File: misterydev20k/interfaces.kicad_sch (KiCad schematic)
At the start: 57 parts, among them J11 Joystick 0, J12 Joystick 1, J4 Micro_SD_Card_Det1, J5 HDMI_A, J6 Grove 1125S-4P, SW2 KEY1, SW3 KEY2, U10 74LCX07, U9 74LCX07

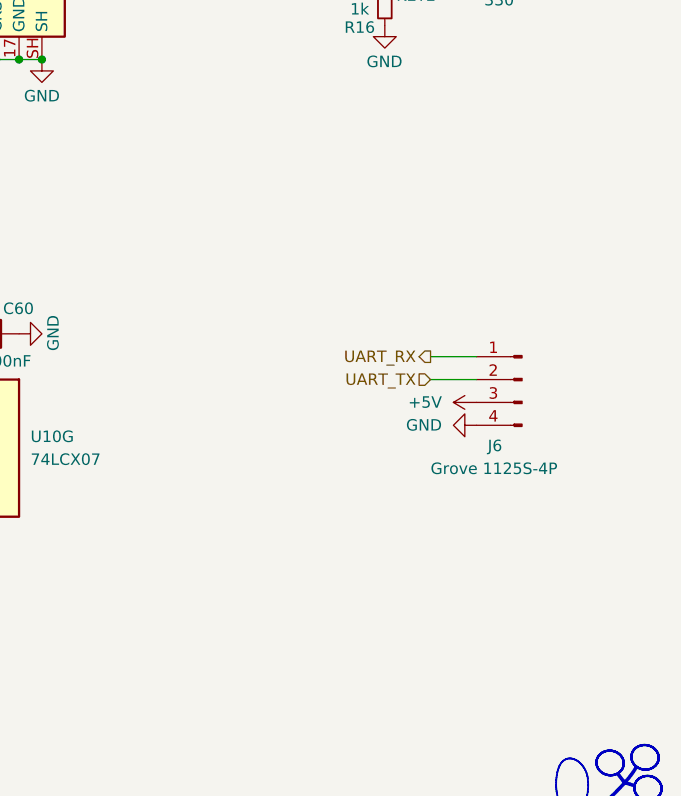
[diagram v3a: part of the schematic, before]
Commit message: Update debug UART wiring
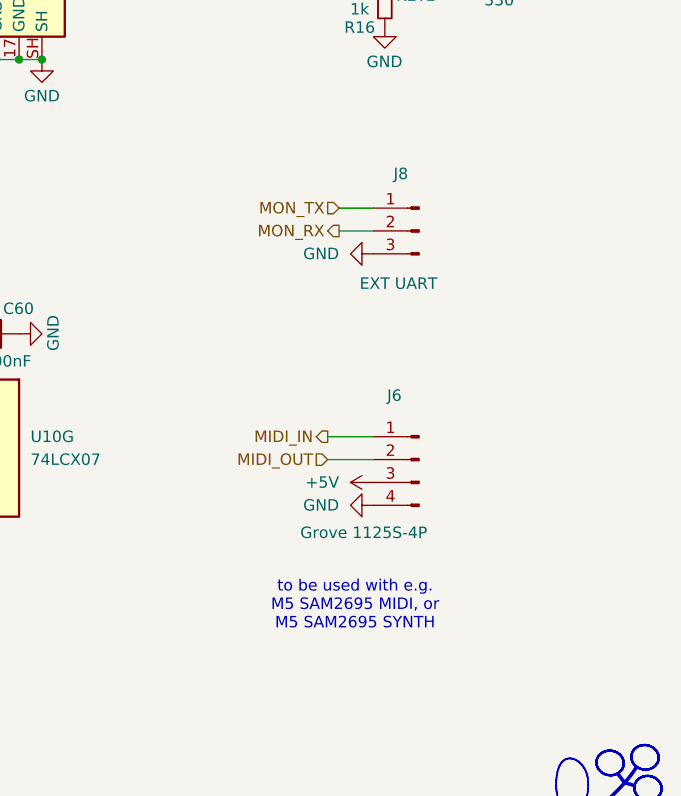
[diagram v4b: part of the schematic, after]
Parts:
- added J8: EXT UART, Connector_PinHeader_2.54mm:PinHeader_1x03_P2.54mm_Vertical, symbol Connector:Conn_01x03_Pin
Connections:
- net GND: now also J8.3 (Pin_3)
- net UART_RX renamed MIDI_IN
- net UART_TX renamed MIDI_OUT
- new net MON_RX: J8.2 (Pin_2)
- new net MON_TX: J8.1 (Pin_1)
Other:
- note added: "to be used with e.g. M5 SAM2695 MIDI, or M5 SAM2695 SYNTH"
- moved on the sheet: J6
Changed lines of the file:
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@@
 		)
 	)
+	(text "to be used with e.g.\nM5 SAM2695 MIDI, or\nM5 SAM2695 SYNTH"
+		(exclude_from_sim no)
+		(at 249.428 152.146 0)
+		(effects
+			(font
+				(size 1.27 1.27)
+			)
+		)
+	)
 	(text "DOWN"
 		(exclude_from_sim no)
@@
 	(wire
 		(pts
-			(xy 257.81 124.46) (xy 262.89 124.46)
+			(xy 246.38 133.35) (xy 251.46 133.35)
 		)
 		(stroke
@@
 	(wire
 		(pts
+			(xy 247.65 107.95) (xy 251.46 107.95)
+		)
+		(stroke
+			(width 0)
+			(type default)
+		)
+	)
+	(wire
+		(pts
 			(xy 54.61 31.75) (xy 55.88 31.75)
 		)
@@
 	(wire
 		(pts
+			(xy 247.65 110.49) (xy 251.46 110.49)
+		)
+		(stroke
+			(width 0)
+			(type default)
+		)
+	)
+	(wire
+		(pts
 			(xy 138.43 128.27) (xy 128.27 128.27)
 		)
@@
 	(wire
 		(pts
-			(xy 257.81 127) (xy 262.89 127)
+			(xy 246.38 135.89) (xy 251.46 135.89)
 		)
 		(stroke
@@
 		)
 	)
-	(hierarchical_label "UART_RX"
+	(hierarchical_label "MIDI_IN"
 		(shape output)
-		(at 257.81 124.46 180)
+		(at 246.38 133.35 180)
 		(effects
 			(font
@@
 		)
 	)
-	(hierarchical_label "UART_TX"
+	(hierarchical_label "MIDI_OUT"
 		(shape input)
-		(at 257.81 127 180)
+		(at 246.38 135.89 180)
 		(effects
 			(font
@@
 		)
 	)
+	(hierarchical_label "MON_RX"
+		(shape output)
+		(at 247.65 110.49 180)
+		(effects
+			(font
+				(size 1.27 1.27)
+			)
+			(justify right)
+		)
+	)
+	(hierarchical_label "MON_TX"
+		(shape input)
+		(at 247.65 107.95 180)
+		(effects
+			(font
+				(size 1.27 1.27)
+			)
+			(justify right)
+		)
+	)
 	(hierarchical_label "SD_DAT3"
 		(shape bidirectional)
@@
 	(symbol
 		(lib_id "power:GND")
-		(at 262.89 132.08 270)
+		(at 251.46 140.97 270)
 		(unit 1)
 		(exclude_from_sim no)
@@
 		(dnp no)
 		(property "Reference" "#PWR0110"
-			(at 256.54 132.08 0)
+			(at 245.11 140.97 0)
 			(effects
 				(font
@@
 		)
 		(property "Value" "GND"
-			(at 259.08 132.08 90)
+			(at 247.65 140.97 90)
 			(effects
 				(font
@@
 		)
 		(property "Footprint" ""
-			(at 262.89 132.08 0)
+			(at 251.46 140.97 0)
 			(effects
 				(font
@@
 		)
 		(property "Datasheet" ""
-			(at 262.89 132.08 0)
+			(at 251.46 140.97 0)
 			(effects
 				(font
@@
 		)
 		(property "Description" "Power symbol creates a global label with name \"GND\" , ground"
-			(at 262.89 132.08 0)
+			(at 251.46 140.97 0)
 			(effects
 				(font
@@
 	(symbol
 		(lib_id "Connector:Conn_01x04_Pin")
-		(at 267.97 127 0)
+		(at 256.54 135.89 0)
 		(mirror y)
 		(unit 1)
@@
 		(dnp no)
 		(property "Reference" "J6"
-			(at 264.16 134.366 0)
+			(at 252.984 128.778 0)
 			(effects
 				(font
@@
 		)
 		(property "Value" "Grove 1125S-4P"
-			(at 257.81 136.906 0)
+			(at 243.332 144.018 0)
 			(effects
 				(font
@@
 		)
 		(property "Footprint" "Connector:NS-Tech_Grove_1x04_P2mm_Vertical"
-			(at 267.97 127 0)
+			(at 256.54 135.89 0)
 			(effects
 				(font
@@
 		)
 		(property "Datasheet" "~"
-			(at 267.97 127 0)
+			(at 256.54 135.89 0)
 			(effects
 				(font
@@
 		)
 		(property "Description" "Generic connector, single row, 01x04, script generated"
-			(at 267.97 127 0)
+			(at 256.54 135.89 0)
 			(effects
 				(font
@@
 		)
 		(property "checked" ""
-			(at 267.97 127 0)
+			(at 256.54 135.89 0)
 			(effects
 				(font
@@
 	)
 	(symbol
+		(lib_id "power:GND")
+		(at 251.46 113.03 270)
+		(mirror x)
+		(unit 1)
+		(exclude_from_sim no)
+		(in_bom yes)
+		(on_board yes)
+		(dnp no)
+		(property "Reference" "#PWR0102"
+			(at 245.11 113.03 0)
+			(effects
+				(font
+					(size 1.27 1.27)
+				)
+				(hide yes)
+			)
+		)
+		(property "Value" "GND"
+			(at 247.65 113.03 90)
+			(effects
+				(font
+					(size 1.27 1.27)
+				)
+				(justify right)
+			)
+		)
+		(property "Footprint" ""
+			(at 251.46 113.03 0)
+			(effects
+				(font
+					(size 1.27 1.27)
+				)
+				(hide yes)
+			)
+		)
+		(property "Datasheet" ""
+			(at 251.46 113.03 0)
+			(effects
+				(font
+					(size 1.27 1.27)
+				)
+				(hide yes)
+			)
+		)
+		(property "Description" "Power symbol creates a global label with name \"GND\" , ground"
+			(at 251.46 113.03 0)
+			(effects
+				(font
+					(size 1.27 1.27)
+				)
+				(hide yes)
+			)
+		)
+		(pin "1"
+		)
+		(instances
+			(project "misterydev20k"
+				(path "/ba62e47e-9e07-4e97-ab08-24b670d50f97/1ae93680-6377-49c6-a9eb-78c5d0ac1afd/1f0ce8d2-82e9-428d-82b0-dc1a063a67f6"
+					(reference "#PWR0102")
+					(unit 1)
+				)
+			)
+		)
+	)
+	(symbol
 		(lib_id "Device:R_Small")
 		(at 191.77 81.28 90)
@@
 	)
 	(symbol
+		(lib_id "Connector:Conn_01x03_Pin")
+		(at 256.54 110.49 0)
+		(mirror y)
+		(unit 1)
+		(exclude_from_sim no)
+		(in_bom yes)
+		(on_board yes)
+		(dnp no)
+		(property "Reference" "J8"
+			(at 254.508 104.14 0)
+			(effects
+				(font
+					(size 1.27 1.27)
+				)
+			)
+		)
+		(property "Value" "EXT UART"
+			(at 254.254 116.332 0)
+			(effects
+				(font
+					(size 1.27 1.27)
+				)
+			)
+		)
+		(property "Footprint" "Connector_PinHeader_2.54mm:PinHeader_1x03_P2.54mm_Vertical"
+			(at 256.54 110.49 0)
+			(effects
+				(font
+					(size 1.27 1.27)
+				)
+				(hide yes)
+			)
+		)
+		(property "Datasheet" "~"
+			(at 256.54 110.49 0)
+			(effects
+				(font
+					(size 1.27 1.27)
+				)
+				(hide yes)
+			)
+		)
+		(property "Description" "Generic connector, single row, 01x03, script generated"
+			(at 256.54 110.49 0)
+			(effects
+				(font
+					(size 1.27 1.27)
+				)
+				(hide yes)
+			)
+		)
+		(pin "3"
+		)
+		(pin "1"
+		)
+		(pin "2"
+		)
+		(instances
+			(project ""
+				(path "/ba62e47e-9e07-4e97-ab08-24b670d50f97/1ae93680-6377-49c6-a9eb-78c5d0ac1afd/1f0ce8d2-82e9-428d-82b0-dc1a063a67f6"
+					(reference "J8")
+					(unit 1)
+				)
+			)
+		)
+	)
+	(symbol
 		(lib_id "Device:R_Small")
 		(at 52.07 58.42 90)
@@
 	(symbol
 		(lib_id "power:+5V")
-		(at 262.89 129.54 90)
+		(at 251.46 138.43 90)
 		(mirror x)
 		(unit 1)
@@
 		(fields_autoplaced yes)
 		(property "Reference" "#PWR0112"
-			(at 266.7 129.54 0)
+			(at 255.27 138.43 0)
 			(effects
 				(font
@@
 		)
 		(property "Value" "+5V"
-			(at 259.08 129.5399 90)
+			(at 247.65 138.4299 90)
 			(effects
 				(font
@@
 		)
 		(property "Footprint" ""
-			(at 262.89 129.54 0)
+			(at 251.46 138.43 0)
 			(effects
 				(font
@@
 		)
 		(property "Datasheet" ""
-			(at 262.89 129.54 0)
+			(at 251.46 138.43 0)
 			(effects
 				(font
@@
 		)
 		(property "Description" "Power symbol creates a global label with name \"+5V\""
-			(at 262.89 129.54 0)
+			(at 251.46 138.43 0)
 			(effects
 				(font

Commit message: Fix JLCPCB footprint offset and rotation
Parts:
- J11, J12: FT Position Offset (none) -> 1,5.5; FT Rotation Offset (none) -> 270; JLCPCB Position Offset 1,5.5 -> (none); JLCPCB Rotation Offset 270 -> (none)
- J5, U10, U9: FT Rotation Offset (none) -> 90
- J6, J8: now left out of the parts list
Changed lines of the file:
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@@
 			)
 		)
+		(property "FT Rotation Offset" "90"
+			(at 76.2 176.53 0)
+			(effects
+				(font
+					(size 1.27 1.27)
+				)
+				(hide yes)
+			)
+		)
 		(pin "8"
 		)
@@
 			)
 		)
+		(property "FT Rotation Offset" "90"
+			(at 207.01 134.62 0)
+			(effects
+				(font
+					(size 1.27 1.27)
+				)
+				(hide yes)
+			)
+		)
 		(pin "8"
 		)
@@
 			)
 		)
+		(property "FT Rotation Offset" "90"
+			(at 64.77 125.73 0)
+			(effects
+				(font
+					(size 1.27 1.27)
+				)
+				(hide yes)
+			)
+		)
 		(pin "8"
 		)
@@
 			)
 		)
+		(property "FT Rotation Offset" "90"
+			(at 184.15 134.62 0)
+			(effects
+				(font
+					(size 1.27 1.27)
+				)
+				(hide yes)
+			)
+		)
 		(pin "8"
 		)
@@
 		(unit 1)
 		(exclude_from_sim no)
-		(in_bom yes)
+		(in_bom no)
 		(on_board yes)
 		(dnp no)
@@
 			)
 		)
+		(property "FT Rotation Offset" "90"
+			(at 207.01 63.5 0)
+			(effects
+				(font
+					(size 1.27 1.27)
+				)
+				(hide yes)
+			)
+		)
 		(pin "8"
 		)
@@
 			)
 		)
+		(property "FT Rotation Offset" "90"
+			(at 76.2 161.29 0)
+			(effects
+				(font
+					(size 1.27 1.27)
+				)
+				(hide yes)
+			)
+		)
 		(pin "8"
 		)
@@
 			)
 		)
+		(property "FT Rotation Offset" "90"
+			(at 64.77 156.21 0)
+			(effects
+				(font
+					(size 1.27 1.27)
+				)
+				(hide yes)
+			)
+		)
 		(pin "8"
 		)
@@
 			)
 		)
+		(property "FT Rotation Offset" "90"
+			(at 64.77 171.45 0)
+			(effects
+				(font
+					(size 1.27 1.27)
+				)
+				(hide yes)
+			)
+		)
 		(pin "8"
 		)
@@
 		(unit 1)
 		(exclude_from_sim no)
-		(in_bom yes)
+		(in_bom no)
 		(on_board yes)
 		(dnp no)
@@
 			)
 		)
+		(property "FT Rotation Offset" "90"
+			(at 76.2 115.57 0)
+			(effects
+				(font
+					(size 1.27 1.27)
+				)
+				(hide yes)
+			)
+		)
 		(pin "8"
 		)
@@
 			)
 		)
+		(property "FT Rotation Offset" "90"
+			(at 87.63 120.65 0)
+			(effects
+				(font
+					(size 1.27 1.27)
+				)
+				(hide yes)
+			)
+		)
 		(pin "8"
 		)
@@
 			)
 		)
-		(property "JLCPCB Rotation Offset" "270"
+		(property "checked" "once"
 			(at 146.05 125.73 0)
 			(effects
@@
 			)
 		)
-		(property "JLCPCB Position Offset" "1,5.5"
+		(property "FT Rotation Offset" "270"
 			(at 146.05 125.73 0)
 			(effects
@@
 			)
 		)
-		(property "checked" "once"
+		(property "FT Position Offset" "1,5.5"
 			(at 146.05 125.73 0)
 			(effects
@@
 			)
 		)
+		(property "FT Rotation Offset" "90"
+			(at 76.2 130.81 0)
+			(effects
+				(font
+					(size 1.27 1.27)
+				)
+				(hide yes)
+			)
+		)
 		(pin "8"
 		)
@@
 			)
 		)
+		(property "FT Rotation Offset" "90"
+			(at 64.77 110.49 0)
+			(effects
+				(font
+					(size 1.27 1.27)
+				)
+				(hide yes)
+			)
+		)
 		(pin "8"
 		)
@@
 			)
 		)
+		(property "FT Rotation Offset" "90"
+			(at 87.63 166.37 0)
+			(effects
+				(font
+					(size 1.27 1.27)
+				)
+				(hide yes)
+			)
+		)
 		(pin "8"
 		)
@@
 			)
 		)
-		(property "JLCPCB Rotation Offset" "270"
+		(property "checked" "once"
 			(at 146.05 171.45 0)
 			(effects
@@
 			)
 		)
-		(property "JLCPCB Position Offset" "1,5.5"
+		(property "FT Rotation Offset" "270"
 			(at 146.05 171.45 0)
 			(effects
@@
 			)
 		)
-		(property "checked" "once"
+		(property "FT Position Offset" "1,5.5"
 			(at 146.05 171.45 0)
 			(effects
@@
 			)
 		)
+		(property "FT Rotation Offset" "90"
+			(at 87.63 181.61 0)
+			(effects
+				(font
+					(size 1.27 1.27)
+				)
+				(hide yes)
+			)
+		)
 		(pin "8"
 		)
@@
 			(at 87.63 135.89 0)
 			(effects
+				(font
+					(size 1.27 1.27)
+				)
+				(hide yes)
+			)
+		)
+		(property "FT Rotation Offset" "90"
+			(at 87.63 135.89 0)
+			(effects

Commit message: Add hyperram
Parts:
- J11, J12: FT Position Offset 1,5.5 -> (none)
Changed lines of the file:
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@@
 			)
 		)
-		(property "FT Position Offset" "1,5.5"
+		(property "FT Position Offset" ""
 			(at 146.05 125.73 0)
 			(effects
@@
 			)
 		)
-		(property "FT Position Offset" "1,5.5"
+		(property "FT Position Offset" ""
 			(at 146.05 171.45 0)
 			(effects

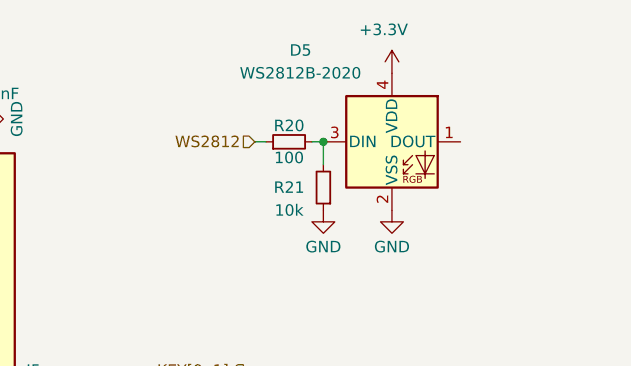
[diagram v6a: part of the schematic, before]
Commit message: Update misterydev20k to v1.1
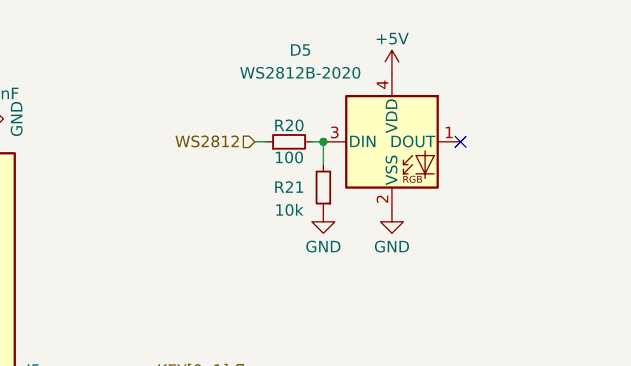
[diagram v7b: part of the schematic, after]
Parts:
- D18: LCSC Part # C2927280 -> C191023
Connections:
- net +3.3V: no longer D5.4 (VDD)
- net +5V: now also D5.4 (VDD)
- no-connect marks 3 -> 4
